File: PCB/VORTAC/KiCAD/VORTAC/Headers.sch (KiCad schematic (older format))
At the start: 9 parts, among them J0 918-418K2023S40001, J1 MillMax_004, J2 MillMax_004, J3 DOCK

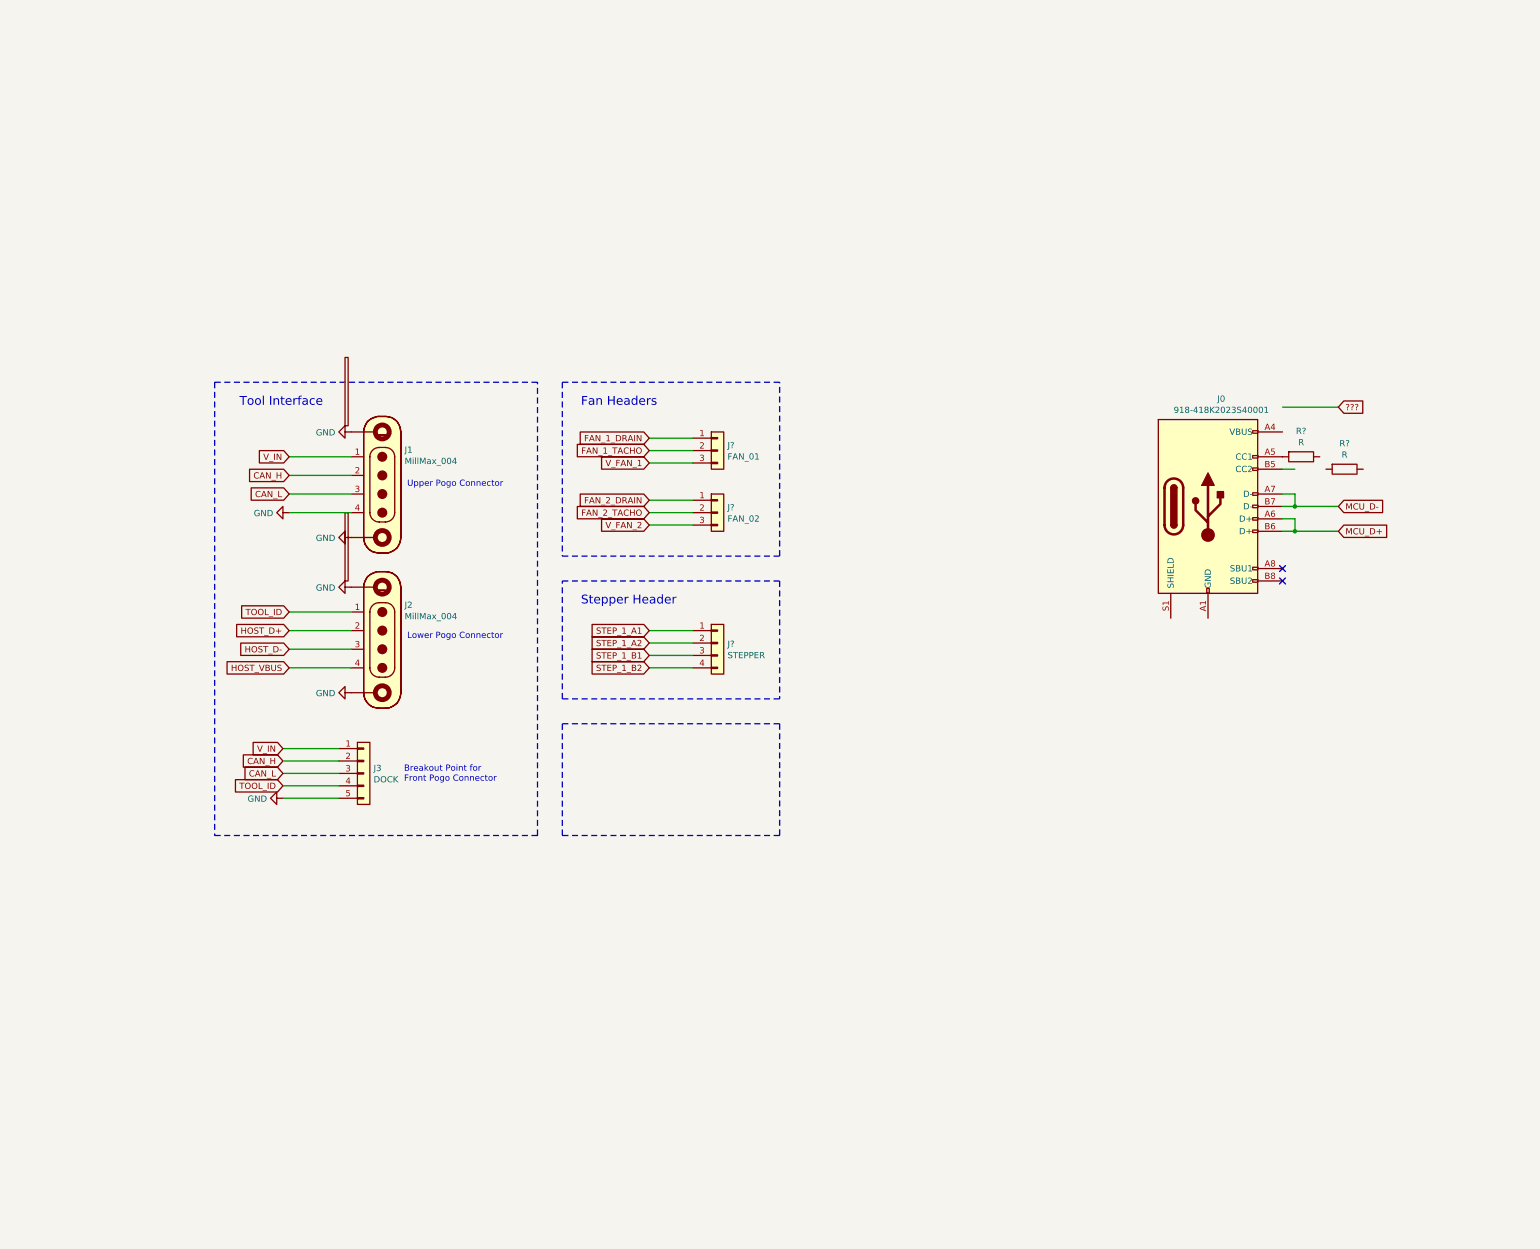
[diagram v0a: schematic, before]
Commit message: pcb, step and headers
-headers schematic updated
-created rough pcb placement of headers
-created step file for inspection in fusion 360
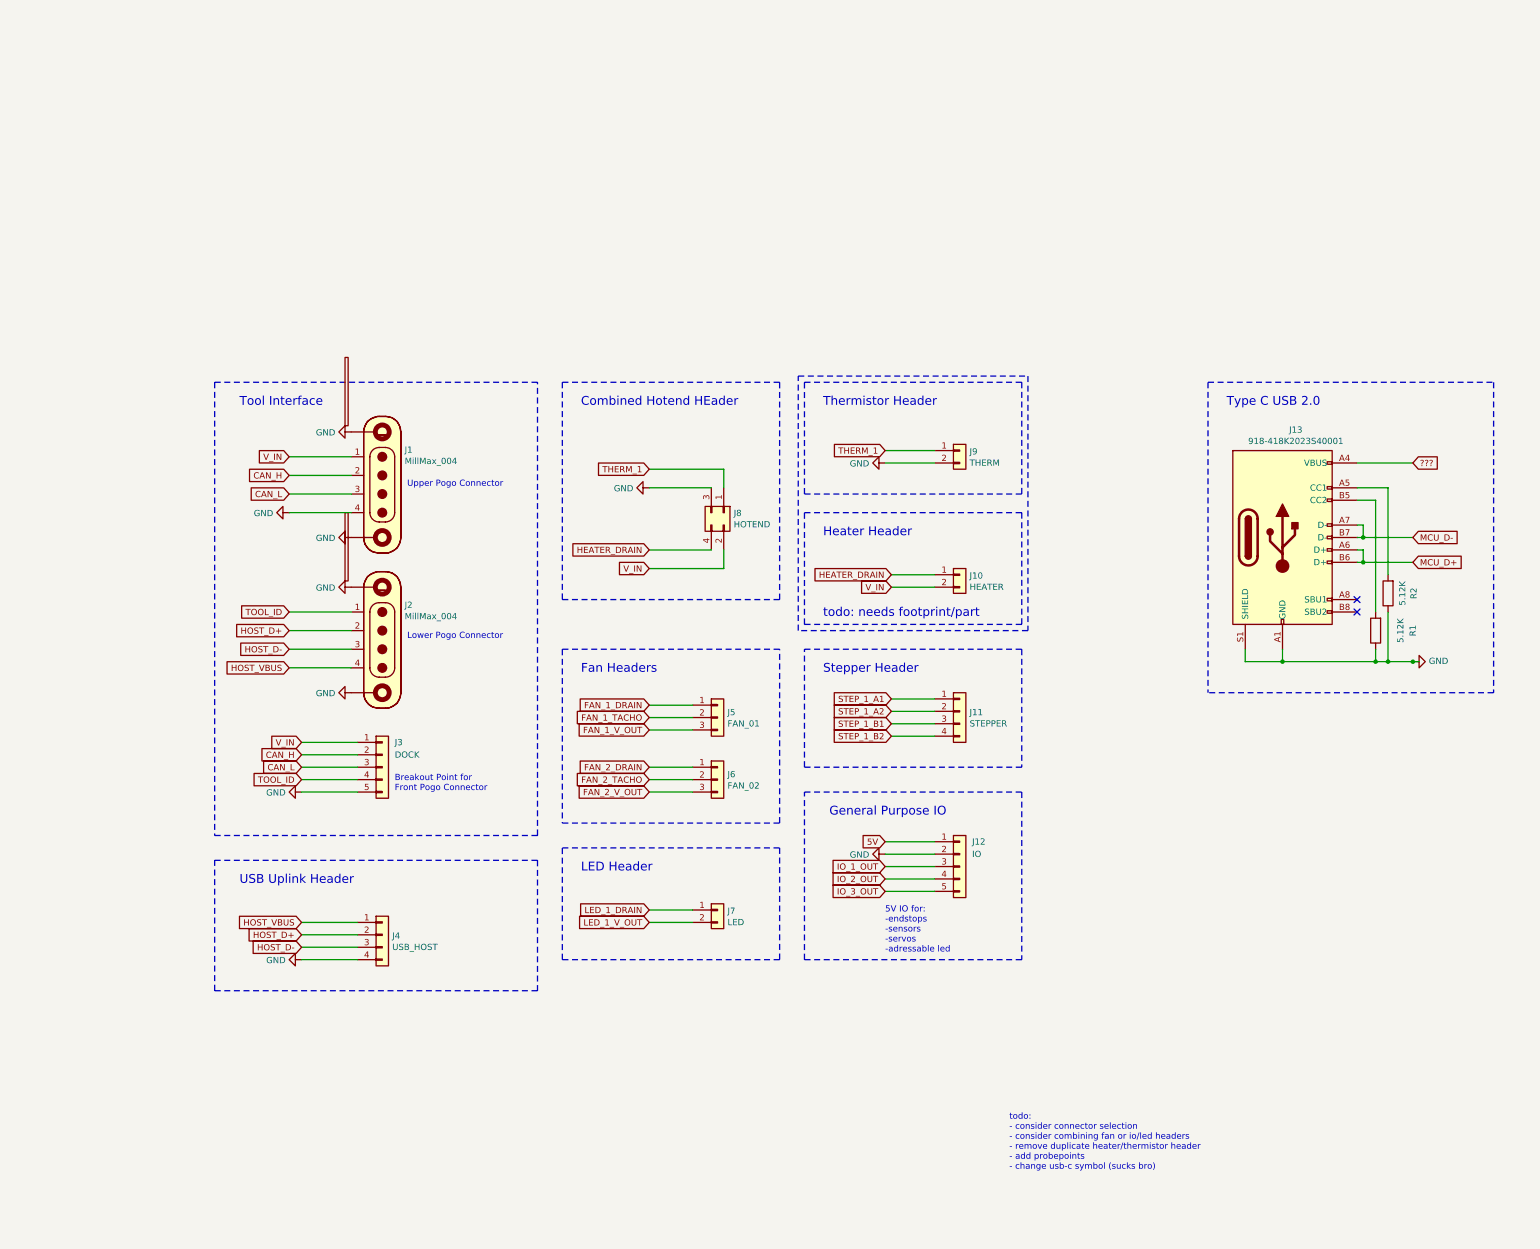
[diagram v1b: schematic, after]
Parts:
- removed R? (x2): R, symbol Device:R
- added J10: HEATER, Connector_Molex:Molex_Micro-Fit_3.0_43045-0412_2x02_P3.00mm_Vertical, symbol Connector_Generic:Conn_01x02
- added J12: IO, Connector_JST:JST_PH_B5B-PH-K_1x05_P2.00mm_Vertical, symbol Connector_Generic:Conn_01x05
- added J4: USB_HOST, Connector_JST:JST_PH_B4B-PH-K_1x04_P2.00mm_Vertical, symbol Connector_Generic:Conn_01x04
- added J7: LED, Connector_JST:JST_PH_B2B-PH-K_1x02_P2.00mm_Vertical, symbol Connector_Generic:Conn_01x02
- added J8: HOTEND, ToolChanger:Molex_Micro-Fit_3.0_43045-0412_2x02_P3.00mm_Vertical, symbol Connector_Generic:Conn_02x02_Odd_Even
- added J9: THERM, Connector_JST:JST_XH_B2B-XH-A_1x02_P2.50mm_Vertical, symbol Connector_Generic:Conn_01x02
- added R1, R2: 5.12K, symbol Device:R
- J11: renamed from J?; footprint Connector_JST:JST_XH_B4B-XH-A_1x04_P2.50mm_Vertical -> Connector_JST:JST_PH_S4B-PH-K_1x04_P2.00mm_Horizontal; LCSC C161871 -> C144395
- J13: renamed from J0; footprint Connector_USB:USB_C_Receptacle_HRO_TYPE-C-31-M-12 -> ToolChanger:USB_C_Receptacle_XKB_U262-16XN-4BVC11
- J3: footprint Connector_JST:JST_XH_B5B-XH-A_1x05_P2.50mm_Vertical -> Connector_JST:JST_PH_B5B-PH-K_1x05_P2.00mm_Vertical; LCSC C161872 -> C157991
- J5, J6: renamed from J?; footprint Connector_JST:JST_XH_B3B-XH-A_1x03_P2.50mm_Vertical -> Connector_JST:JST_PH_B3B-PH-K_1x03_P2.00mm_Vertical
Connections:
- net labels added: 5V, FAN_1_V_OUT, FAN_2_V_OUT, HEATER_DRAIN, IO_1_OUT, IO_2_OUT, IO_3_OUT, LED_1_DRAIN, LED_1_V_OUT, THERM_1
- net labels removed: V_FAN_1, V_FAN_2
- wire segments 33 -> 66
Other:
- note added: "5V IO for:\n-endstops\n-sensors\n-servos\n-adressable led"
- note added: "Combined Hotend HEader"
- note added: "General Purpose IO"
- note added: "Heater Header"
- note added: "LED Header"
- note added: "Thermistor Header"
- note added: "Type C USB 2.0"
- note added: "USB Uplink Header"
- note added: "todo: needs footprint/part"
- note added: "todo:\n- consider connector selection\n- consider combining fan or io/led headers\n- remove duplicate heater/thermistor header\n- add probepoints\n- change usb-c symbol (sucks bro)"
- moved on the sheet: J11, J13, J3, J5, J6

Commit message: Auto stash before merge of "main" and "origin/main"
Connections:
- net 5V: now also J4.1 (Pin_1)
- net GND: no longer J4.4 (Pin_4)
- net HOST_D+: no longer J4.2 (Pin_2)
- net HOST_D-: no longer J4.3 (Pin_3)
- net HOST_VBUS: no longer names the net of J2.4
- net HOST_VBUS: no longer J4.1 (Pin_1)
- net MCU_D+ renamed USBMCU_D+
- net MCU_D- renamed USBMCU_D-
- new net USBH_D+: J4.2 (Pin_2)
- new net USBH_D-: J4.3 (Pin_3)
- new net USBH_DRAIN: J4.4 (Pin_4)
- no-connect marks 2 -> 3
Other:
- moved on the sheet: J10, J11, J12, J5, J6, J7, J9

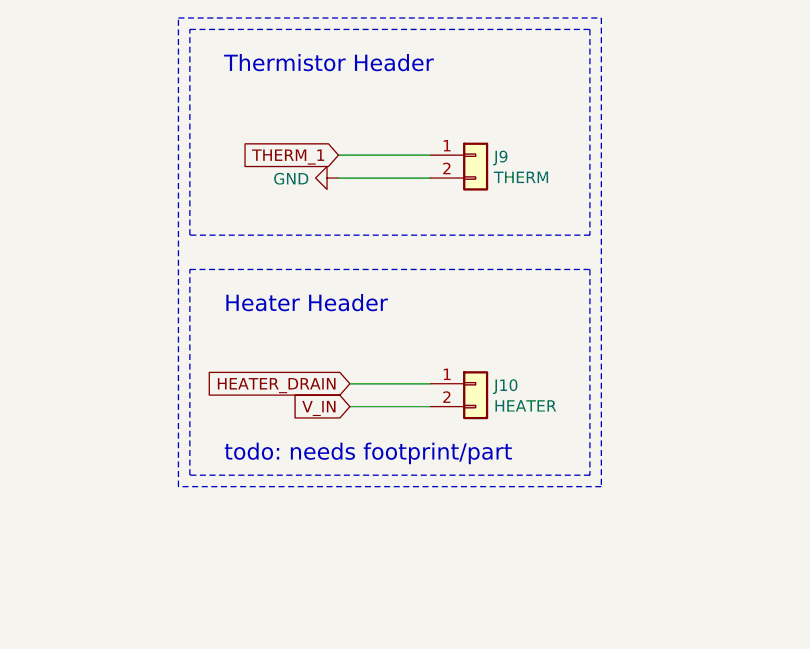
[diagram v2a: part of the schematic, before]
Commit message: updated schematics
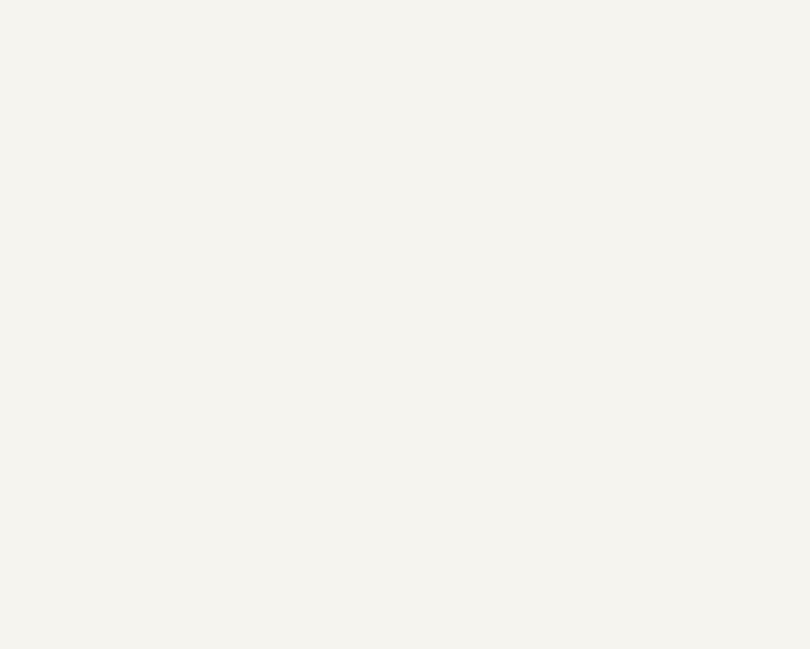
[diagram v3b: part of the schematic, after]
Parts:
- removed J10: HEATER, Connector_Molex:Molex_Micro-Fit_3.0_43045-0412_2x02_P3.00mm_Vertical, symbol Connector_Generic:Conn_01x02
- removed J9: THERM, Connector_JST:JST_XH_B2B-XH-A_1x02_P2.50mm_Vertical, symbol Connector_Generic:Conn_01x02
- R1, R2: footprint (none) -> Resistor_SMD:R_0402_1005Metric
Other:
- note removed: "Heater Header"
- note removed: "Thermistor Header"
- note removed: "todo: needs footprint/part"
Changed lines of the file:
@@
 Wire Notes Line
 	3500 2650 3500 4050
-Wire Notes Line
-	3450 -2250 5200 -2250
-Wire Notes Line
-	5200 -2250 5200 -1350
-Wire Notes Line
-	5200 -1350 3450 -1350
-Wire Notes Line
-	3450 -1350 3450 -2250
 Text GLabel 1400 5050 0    50   Input ~ 0
 5V
@@
 Wire Notes Line
 	700  5600 700  4550
-$Comp
-L Connector_Generic:Conn_01x02 J9
-U 1 1 61496B79
-P 4700 -1700
-F 0 "J9" H 4780 -1708 50  0000 L CNN
-F 1 "THERM" H 4780 -1799 50  0000 L CNN
-F 2 "Connector_JST:JST_XH_B2B-XH-A_1x02_P2.50mm_Vertical" H 4700 -1700 50  0001 C CNN
-F 3 "https://www.lcsc.com/product-detail/Wire-To-Board-Wire-To-Wire-Connector_JST-Sales-America-B2B-XH-A-LF-SN_C158012.html" H 4700 -1700 50  0001 C CNN
-F 4 "C158012" H 4700 -1700 50  0001 C CNN "LCSC"
-	1    4700 -1700
-	1    0    0    -1
-$EndComp
-$Comp
-L Connector_Generic:Conn_01x02 J10
-U 1 1 614987F9
-P 4700 -700
-F 0 "J10" H 4780 -708 50  0000 L CNN
-F 1 "HEATER" H 4780 -799 50  0000 L CNN
-F 2 "Connector_Molex:Molex_Micro-Fit_3.0_43045-0412_2x02_P3.00mm_Vertical" H 4700 -700 50  0001 C CNN
-F 3 "https://www.lcsc.com/product-detail/Wire-To-Board-Wire-To-Wire-Connector_MOLEX-430450412_C277721.html" H 4700 -700 50  0001 C CNN
-F 4 "C277721" H 4700 -700 50  0001 C CNN "LCSC"
-	1    4700 -700
-	1    0    0    -1
-$EndComp
 $Comp
 L Connector_Generic:Conn_01x04 J4
@@
 	1    0    0    -1
 $EndComp
-Wire Notes Line
-	5200 -1200 5200 -300
-Wire Notes Line
-	5200 -300 3450 -300
-Wire Notes Line
-	3450 -300 3450 -1200
-Wire Notes Line
-	3450 -1200 5200 -1200
-Text GLabel 4150 -700 0    50   Input ~ 0
-HEATER_DRAIN
-Text GLabel 4150 -600 0    50   Input ~ 0
-V_IN
-Text Notes 3600 -1000 0    71   ~ 0
-Heater Header
-Wire Wire Line
-	4150 -700 4500 -700
-Wire Wire Line
-	4500 -600 4150 -600
-Text Notes 3600 -350 0    71   ~ 0
-todo: needs footprint/part
 Wire Wire Line
 	9000 2950 9300 2950
@@
 F 0 "R2" V 9943 2400 50  0000 C CNN
 F 1 "5.12K" V 10034 2400 50  0000 C CNN
-F 2 "" V 10080 2400 50  0001 C CNN
+F 2 "Resistor_SMD:R_0402_1005Metric" V 10080 2400 50  0001 C CNN
 F 3 "~" H 10150 2400 50  0001 C CNN
 	1    10150 2400
@@
 F 0 "R1" V 9750 2700 50  0000 C CNN
 F 1 "5.12K" V 9850 2700 50  0000 C CNN
-F 2 "" V 9980 2700 50  0001 C CNN
+F 2 "Resistor_SMD:R_0402_1005Metric" V 9980 2700 50  0001 C CNN
 F 3 "~" H 10050 2700 50  0001 C CNN
 	1    10050 2700
@@
 	1    0    0    -1
 $EndComp
-Text Notes 3600 -2050 0    71   ~ 0
-Thermistor Header
-Text GLabel 4100 -1700 0    50   Input ~ 0
-THERM_1
-$Comp
-L power:GND #PWR09
-U 1 1 614EC081
-P 4100 -1600
-F 0 "#PWR09" H 4100 -1850 50  0001 C CNN
-F 1 "GND" V 4105 -1728 50  0000 R CNN
-F 2 "" H 4100 -1600 50  0001 C CNN
-F 3 "" H 4100 -1600 50  0001 C CNN
-	1    4100 -1600
-	0    1    1    0
-$EndComp
-Wire Wire Line
-	4100 -1700 4500 -1700
-Wire Wire Line
-	4500 -1600 4100 -1600
 Text Notes 900  4750 0    71   ~ 0
 USB Uplink Header
@@
 F 1 "HOTEND" V 4895 1830 50  0000 L CNN
 F 2 "ToolChanger:Molex_Micro-Fit_3.0_43045-0412_2x02_P3.00mm_Vertical" H 4800 1750 50  0001 C CNN
-F 3 "https://www.lcsc.com/product-detail/Wire-To-Board-Wire-To-Wire-Connector_MOLEX-430450412_C277721.html" H 4800 1750 50  0001 C CNN
+F 3 "~" H 4800 1750 50  0001 C CNN
 F 4 "C277721" V 4800 1750 50  0001 C CNN "LCSC"
 	1    4800 1750
@@
 Text Notes 3650 900  0    71   ~ 0
 Combined Hotend HEader
-Wire Notes Line
-	5250 -2300 5250 -250
-Wire Notes Line
-	5250 -250 3400 -250
-Wire Notes Line
-	3400 -250 3400 -2300
-Wire Notes Line
-	3400 -2300 5250 -2300
 Text Notes 7050 7050 0    50   ~ 0
 todo:\n- consider connector selection\n- consider combining fan or io/led headers\n- remove duplicate heater/thermistor header\n- add probepoints\n- change usb-c symbol (sucks bro)

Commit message: Schematic and Lib Updates
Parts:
- added C11: 0.1uF, Capacitor_SMD:C_0402_1005Metric_Pad0.74x0.62mm_HandSolder, symbol Device:C_Small
- added J10: FAN_01_V, Connector_PinHeader_1.27mm:PinHeader_2x03_P1.27mm_Vertical, symbol Connector_Generic:Conn_02x03_Odd_Even
- added J14: FAN_02_V, Connector_PinHeader_1.27mm:PinHeader_2x03_P1.27mm_Vertical, symbol Connector_Generic:Conn_02x03_Odd_Even
- added J15: LED_V, Connector_PinHeader_1.27mm:PinHeader_2x03_P1.27mm_Vertical, symbol Connector_Generic:Conn_02x03_Odd_Even
- added J16: THERM_R, Connector_PinHeader_1.27mm:PinHeader_2x02_P1.27mm_Vertical, symbol Connector_Generic:Conn_02x02_Odd_Even
- added J9: Conn_02x03_Odd_Even, ToolChanger:Molex_Micro-Fit_3.0_43045-0612_2x03_P3.00mm_Vertical, symbol Connector_Generic:Conn_02x03_Odd_Even
- added R28: 10K, Resistor_SMD:R_0402_1005Metric, symbol Device:R_Small
- J8: LCSC C277721 -> (none)
- R1, R2: symbol Device:R -> Device:R_Small
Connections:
- net 5V: now also J10.3 (Pin_3), J14.3 (Pin_3), J15.3 (Pin_3)
- net CAN_H: now also J9.3 (Pin_3); no longer J3.2 (Pin_2)
- net CAN_L: now also J9.4 (Pin_4); no longer J3.3 (Pin_3)
- net FAN_1_V_OUT: now also J10.2 (Pin_2), J10.4 (Pin_4), J10.6 (Pin_6)
- net FAN_2_V_OUT: now also J14.2 (Pin_2), J14.4 (Pin_4), J14.6 (Pin_6)
- net GND: now also J8.4 (Pin_4), C11.2; no longer J3.5 (Pin_5), J8.3 (Pin_3)
- net HEATER_DRAIN: now also J8.2 (Pin_2); no longer J8.4 (Pin_4)
- net LED_1_V_OUT: now also J15.2 (Pin_2), J15.4 (Pin_4), J15.6 (Pin_6)
- net THERM_1: now also J8.3 (Pin_3); no longer J8.1 (Pin_1)
- net TOOL_ID: now also J9.5 (Pin_5); no longer J3.4 (Pin_4)
- net V_IN: now also J8.1 (Pin_1), J10.1 (Pin_1), J14.1 (Pin_1), J15.1 (Pin_1); no longer J3.1 (Pin_1), J8.2 (Pin_2)
- new net 3.3V: J10.5 (Pin_5), J14.5 (Pin_5), J15.5 (Pin_5)
- new net DOCK_GND: J9.2 (Pin_2)
- new net DOCK_V_IN: J9.1 (Pin_1)
- no-connect marks 3 -> 4
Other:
- note added: "Fan Power Selector"
- note added: "LED Power Selector"
- moved on the sheet: J1, J11, J12, J13, J2, J3, J4, J5, J6, J7, J8, R1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

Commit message: pushie
updates and stuff
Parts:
- removed C11: 0.1uF, Capacitor_SMD:C_0402_1005Metric_Pad0.74x0.62mm_HandSolder, symbol Device:C_Small
- removed J3: DOCK, Connector_JST:JST_PH_B5B-PH-K_1x05_P2.00mm_Vertical, symbol Connector_Generic:Conn_01x05
- removed R28: 10K, Resistor_SMD:R_0402_1005Metric, symbol Device:R_Small
- added J3: DEBUG, Connector_PinHeader_1.27mm:PinHeader_2x03_P1.27mm_Vertical, symbol Connector_Generic:Conn_02x03_Odd_Even
- added R3: 1K .1%, Resistor_SMD:R_0402_1005Metric, symbol Device:R_Small
- added R4: 4.7K .1%, Resistor_SMD:R_0402_1005Metric, symbol Device:R_Small
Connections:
- net 3.3V is gone; now on net 5V: J10.5 (Pin_5), J14.5 (Pin_5), J15.5 (Pin_5)
- net 5V: no longer J10.3 (Pin_3), J14.3 (Pin_3), J15.3 (Pin_3)
- net AREF: now also J16.2 (Pin_2), J16.4 (Pin_4)
- net STEP_1_A1: now also J11.2 (Pin_2); no longer J11.1 (Pin_1)
- net STEP_1_A2: now also J11.1 (Pin_1); no longer J11.2 (Pin_2)
- net at J16.1 (Pin_1): now also R3.1
- net at J16.3 (Pin_3): now also R4.1
- new net 12V: J10.3 (Pin_3), J14.3 (Pin_3), J15.3 (Pin_3)
- new net THERM_1_UP: R3.2, R4.2
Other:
- note added: "Combined Hotend Header"
- note added: "Debug & Programmin Header"
- note added: "Thermistor Pullup Selector"
- note removed: "Combined Hotend HEader"
- moved on the sheet: J10, J14, J15, J16, J5, J6, J7, J8

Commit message: progress
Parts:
- added D5: D_Schottky, symbol Device:D_Schottky
- added H1, H2: M3, MountingHole:MountingHole_3mm_Pad_Via, symbol Mechanical:MountingHole_Pad
- added JP1, JP2: SolderJumper_2_Bridged, ToolChanger:SolderJumper_Hex_Bridged_Pad, symbol Jumper:SolderJumper_2_Bridged
- added JP3, JP4: SolderJumper_2_Open, ToolChanger:SolderJumper_Hex_Open_Pad, symbol Jumper:SolderJumper_2_Open
- J2: renamed from J9; value Conn_02x03_Odd_Even -> Molex Micro Fit 3.0; symbol Connector_Generic:Conn_02x03_Odd_Even -> Connector_Generic:Conn_02x03_Top_Bottom
- J6: renamed from J8; symbol Connector_Generic:Conn_02x02_Odd_Even -> Connector_Generic:Conn_02x02_Top_Bottom
- renumbered J3 to J1, J14 to J11, J15 to J12, J16 to J13, J13 to J14, J11 to J15, J12 to J16, J1 to J3, J2 to J4, J4 to J5, J5 to J7, J6 to J8, J7 to J9, R3 to R1, R4 to R2, R1 to R3, R2 to R4
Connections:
- net labels added: HOST_USB_D+, HOST_USB_D-, HOST_USB_DRAIN, THERM_1_OUT, TOOL_DATA_H, TOOL_DATA_L, USB_D+, USB_D-
- net labels removed: ???, HOST_D+, HOST_D-, THERM_1, USBH_D+, USBH_D-, USBH_DRAIN, USBMCU_D+, USBMCU_D-
- no-connect marks 4 -> 3
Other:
- note added: "Debug Header"
- note added: "Host USB Header"
- note added: "Uplink USB Port \nfor nozzlecams"
- note removed: "Debug & Programmin Header"
- note removed: "USB Uplink Header"
- moved on the sheet: J1, J10, J11, J12, J13, J14, J15, J16, J2, J3, J4, J5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

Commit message: progress
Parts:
- D5: footprint (none) -> Diode_SMD:D_SOD-123; LCSC (none) -> C37049
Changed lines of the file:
@@
 encoding utf-8
 Sheet 2 4
-Title ""
-Date ""
-Rev ""
-Comp ""
-Comment1 ""
-Comment2 ""
-Comment3 ""
-Comment4 ""
+Title "Headers & Tool Interfacing"
+Date "2021-10-17"
+Rev "0.0"
+Comp "VORTAC DESIGN"
+Comment1 "!! wip untested revesion !!"
+Comment2 "Designed to be used with Klipper Firmware"
+Comment3 "Canbus Networked Smart Tool Board"
+Comment4 "-- VORTAC PCB --"
 $EndDescr
 $Comp
@@
 Text Notes 3550 900  0    71   ~ 0
 Combined Hotend Header
-Text Notes 7050 7050 0    50   ~ 0
+Text Notes 9200 7050 0    50   ~ 0
 todo:\n- consider connector selection\n- consider combining fan or io/led headers\n- remove duplicate heater/thermistor header\n- add probepoints\n- change usb-c symbol (sucks bro)
 NoConn ~ 1400 1350
@@
 F 0 "D5" H 2200 5733 50  0000 C CNN
 F 1 "D_Schottky" H 2200 5824 50  0000 C CNN
-F 2 "" H 2200 5950 50  0001 C CNN
-F 3 "~" H 2200 5950 50  0001 C CNN
+F 2 "Diode_SMD:D_SOD-123" H 2200 5950 50  0001 C CNN
+F 3 "https://www.lcsc.com/product-detail/Schottky-Barrier-Diodes-SBD_MDD-Microdiode-Electronics-DSK14_C37049.html" H 2200 5950 50  0001 C CNN
+F 4 "C37049" H 2200 5950 50  0001 C CNN "LCSC"
 	1    2200 5950
 	-1   0    0    1
